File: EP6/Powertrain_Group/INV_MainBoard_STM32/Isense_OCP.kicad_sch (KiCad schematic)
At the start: 42 parts, among them J13 motorTemp, J5 current_DC, J6 to PhaseIsense, Q3 2N7002, Q4 2N7002, U15 LM393, U5 NE555D

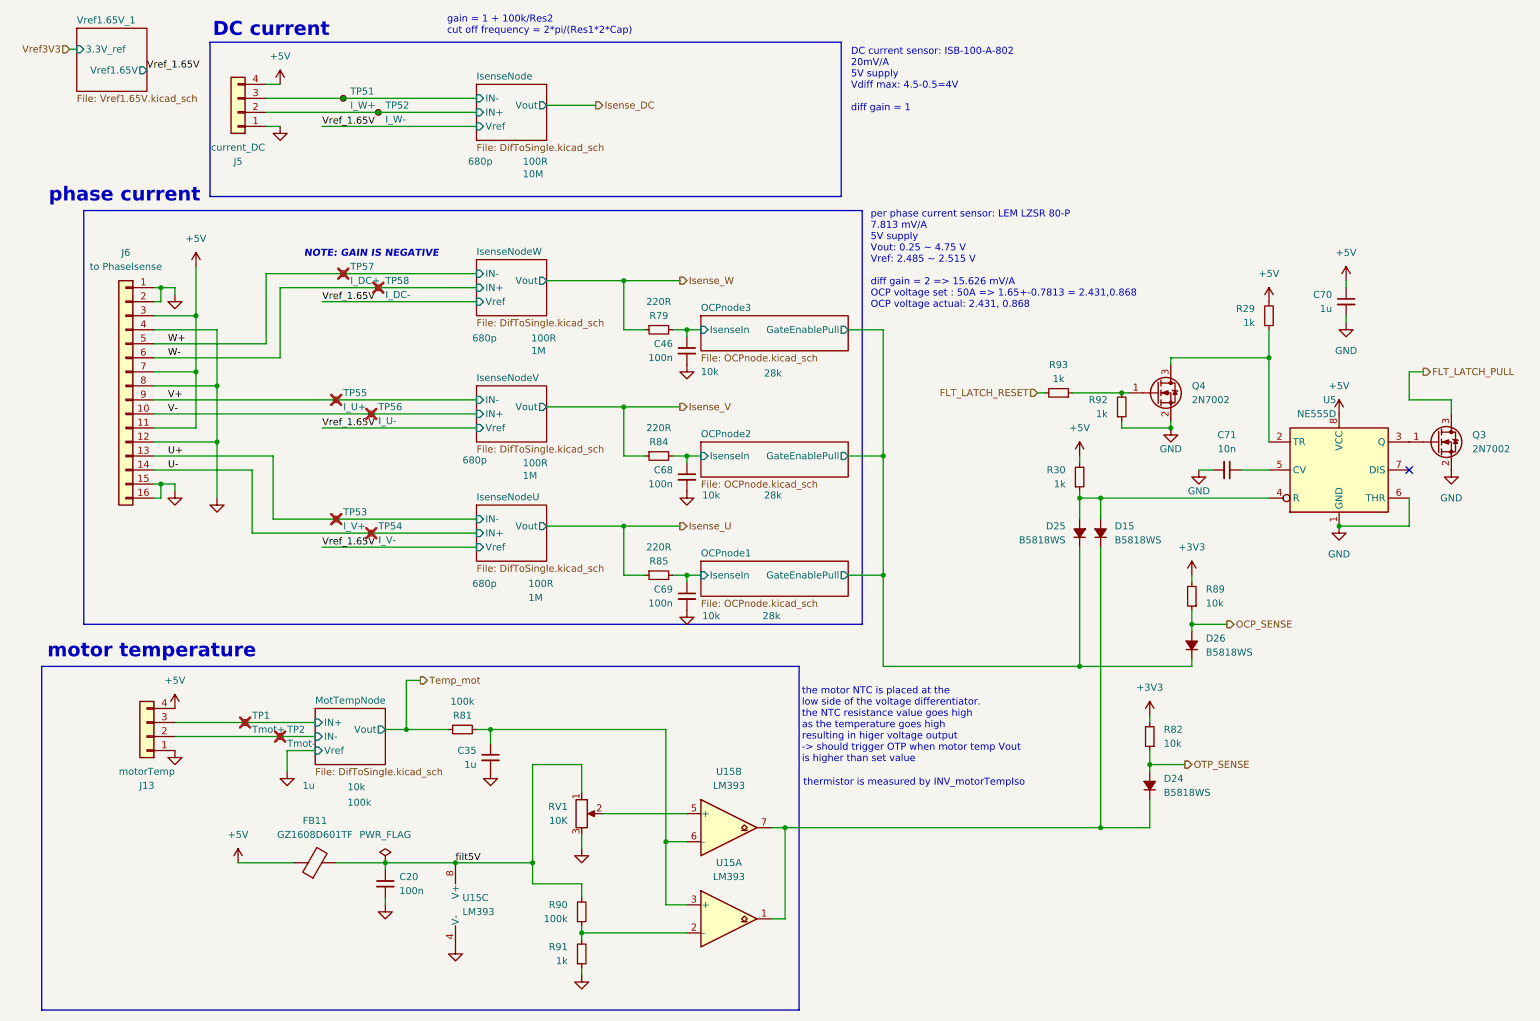
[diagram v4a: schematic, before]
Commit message: update INV_MainBoard_STM32 to V3.1
V3.1 fix R93 to 100R
     add led for OCP, OTP flt
     add default Res for OTP threshold
     add gnd pins for testing
     fix latch circuit
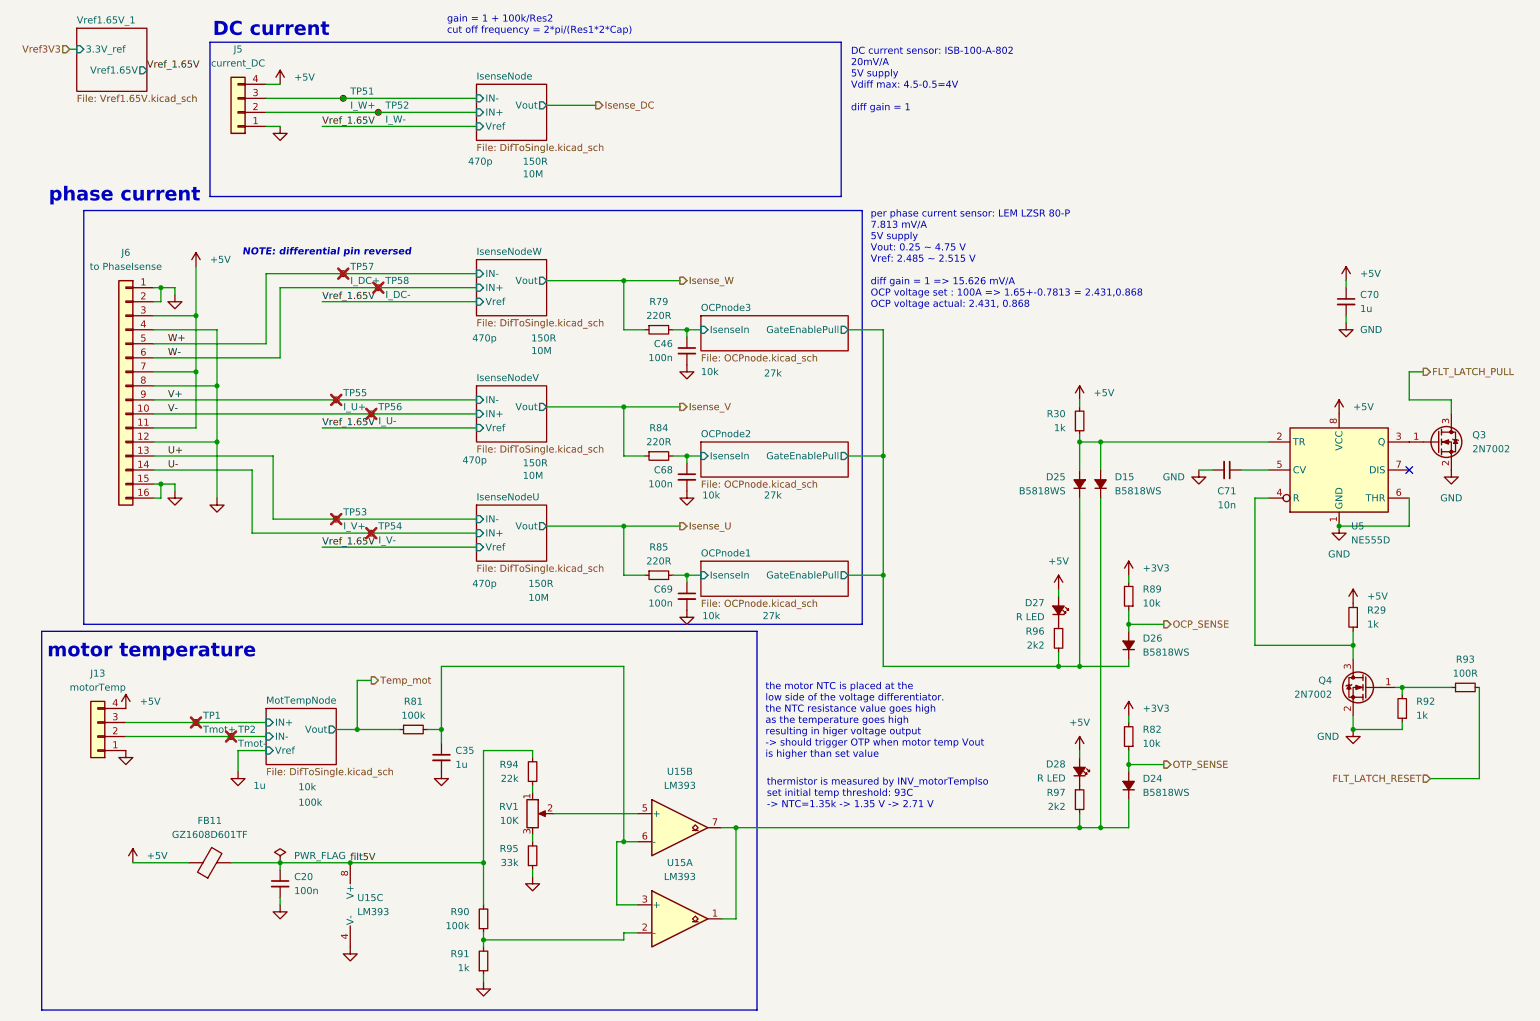
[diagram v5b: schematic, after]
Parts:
- added D27, D28: R LED, LED_SMD:LED_0603_1608Metric, symbol Device:LED_Small_Filled
- added R94: 22k, Resistor_SMD:R_0402_1005Metric, symbol Device:R_Small
- added R95: 33k, Resistor_SMD:R_0402_1005Metric, symbol Device:R_Small
- added R96, R97: 2k2, Resistor_SMD:R_0402_1005Metric, symbol Device:R_Small
- R93: value 1k -> 100R
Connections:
- net +5V: now also D27.2 (A), D28.2 (A)
- net GND: now also R95.1; no longer RV1.3
- net OCPnode1/GateEnablePull: now also R96.2
- net filt5V: now also R94.2; no longer RV1.1
- net at D15.1 (K), D24.1 (K), U15.1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: now also R97.2
- net at Q4.3 (D), R29.1: now also U5.4 (R); no longer U5.2 (TR)
- net at D15.2 (A), D25.2 (A), R30.1: now also U5.2 (TR); no longer U5.4 (R)
- new net: R95.2, RV1.3
- new net: D28.1 (K), R97.1
- new net: D27.1 (K), R96.1
- new net: R94.1, RV1.1
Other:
- note added: "NOTE: differential pin reversed"
- note added: "per phase current sensor: LEM LZSR 80-P 7.813 mV/A 5V supply Vout: 0.25 ~ 4.75 V Vref: 2.485 ~ 2.515 V diff gain = 1 => 15.626 mV/A OCP voltage set : 100A => 1.65+-0.7813 = 2.431,0.868 OCP voltage actual: 2.431, 0.868"
- note added: "thermistor is measured by INV_motorTempIso set initial temp threshold: 93C -> NTC=1.35k -> 1.35 V -> 2.71 V"
- note removed: "NOTE: GAIN IS NEGATIVE"
- note removed: "per phase current sensor: LEM LZSR 80-P 7.813 mV/A 5V supply Vout: 0.25 ~ 4.75 V Vref: 2.485 ~ 2.515 V diff gain = 2 => 15.626 mV/A OCP voltage set : 50A => 1.65+-0.7813 = 2.431,0.868 OCP voltage actual: 2.431, 0.868"
- note removed: "thermistor is measured by INV_motorTempIso"
- moved on the sheet: C20, C35, D15, D24, D25, D26, FB11, J13, Q4, R29, R30, R81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
